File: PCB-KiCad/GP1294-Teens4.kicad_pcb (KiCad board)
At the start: 2 copper layers, 178.3 x 100.1 mm, 98 parts, among them IC1 74132D, IC3 ZXBM5210, Q1 ALS-PDIC144, SW1 SW_DPDT_x2, SW2 SW_DPDT_x2, SW3 SW_DPDT_x2, SW4 SW_DPDT_x2, SW5 SW_DPDT_x2, U10 TSOP34S40F, U3 R-78B5.0-2.0, U5 ATtiny84A-P, U6 74HC165, U7 74HC165, U8 CS8421

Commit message: Fixed merge fail.
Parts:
- removed the R2 at (104.5, 61.5)
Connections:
- U1 pad 2: F1 -> unconnected-(U1-F+-Pad2)
- U1 pad 29: F2 -> unconnected-(U1-F--Pad29)
- U1 pad 3: F1 -> unconnected-(U1-F+-Pad3)
- U1 pad 30: F2 -> unconnected-(U1-F--Pad30)
- U1 pad 31: F2 -> unconnected-(U1-F--Pad31)
- U1 pad 4: F1 -> unconnected-(U1-F+-Pad4)
- U1 pad 9: Net-(U1-TEST) -> +3.3V

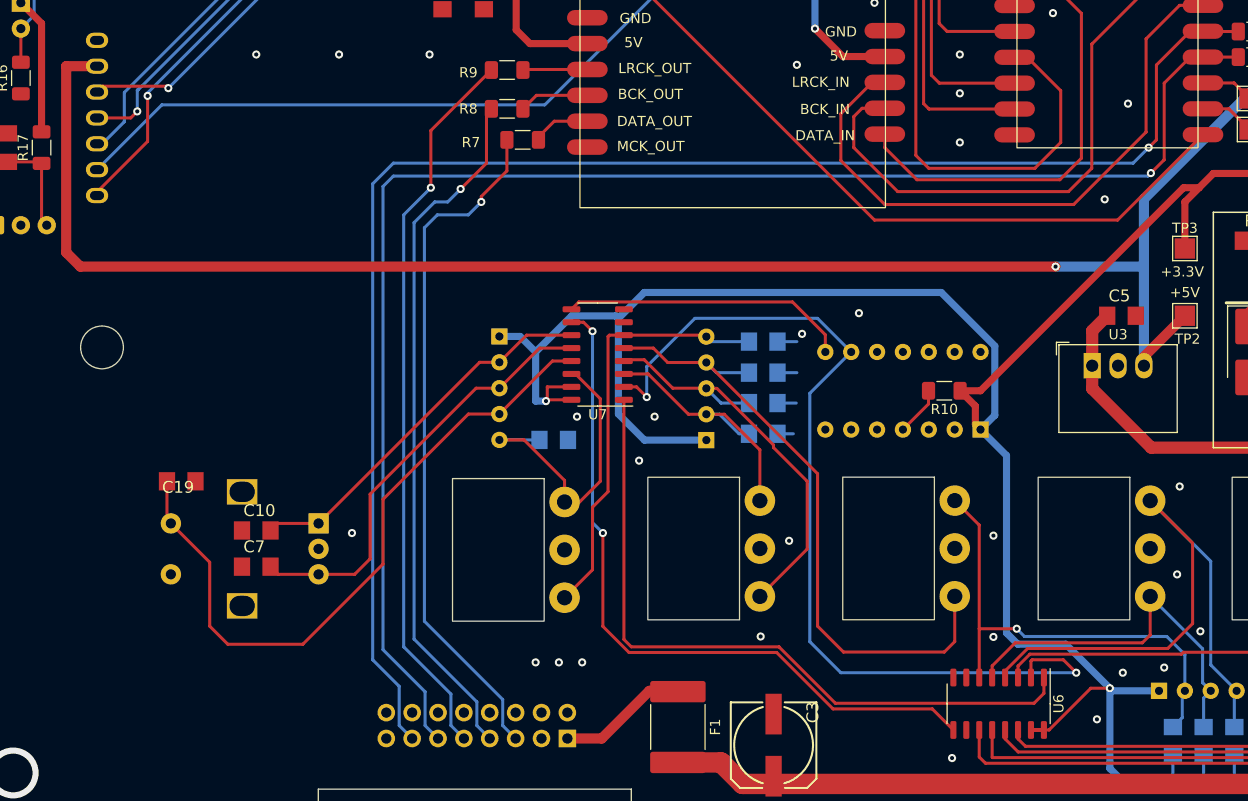
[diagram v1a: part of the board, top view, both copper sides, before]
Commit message: Fixed i2c..
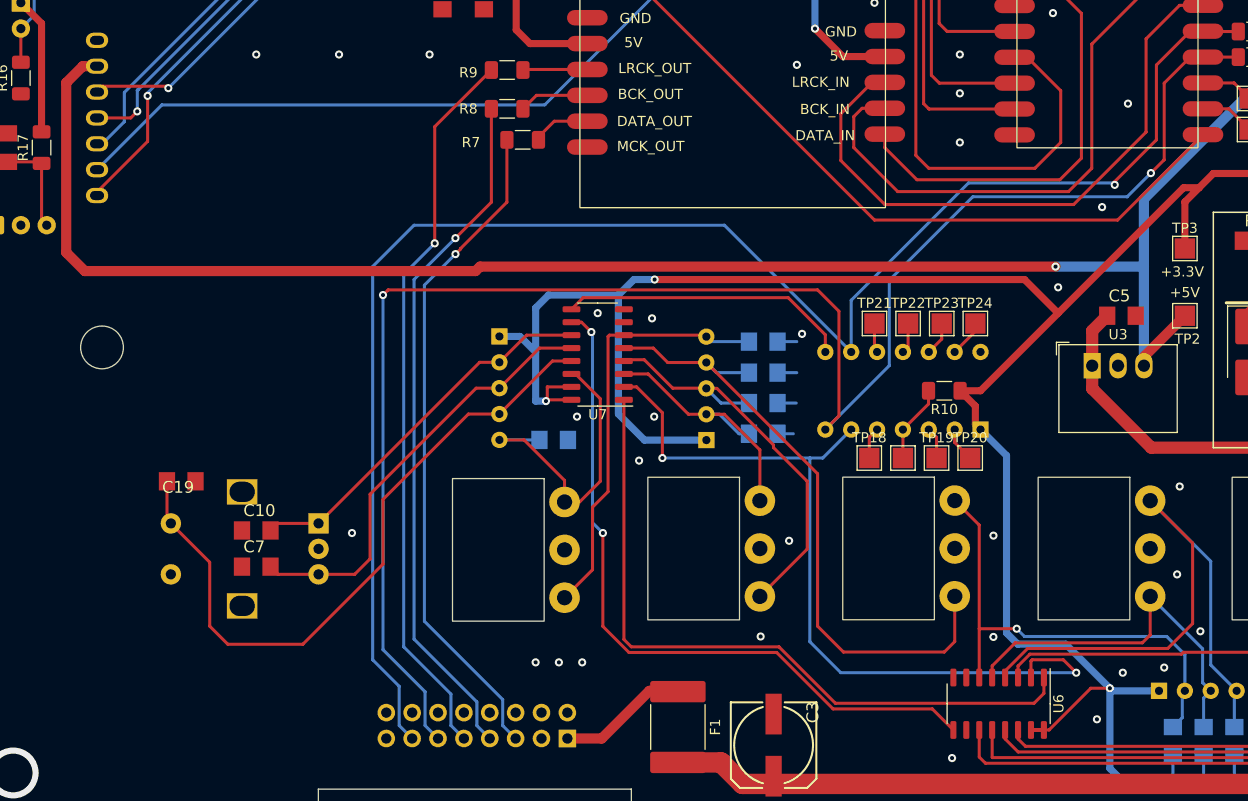
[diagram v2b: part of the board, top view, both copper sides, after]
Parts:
- added TP17: PB3, TestPoint:TestPoint_Pad_2.0x2.0mm, F.Cu at (151.4, 116.1)
- added TP18: PB2, TestPoint:TestPoint_Pad_2.0x2.0mm, F.Cu at (148.1, 116.1)
- added TP19: PB1, TestPoint:TestPoint_Pad_2.0x2.0mm, F.Cu at (154.7, 116.1)
- added TP20: PB0, TestPoint:TestPoint_Pad_2.0x2.0mm, F.Cu at (158.0, 116.1)
- added TP21: PA3, TestPoint:TestPoint_Pad_2.0x2.0mm, F.Cu at (148.6, 102.9)
- added TP22: PA2, TestPoint:TestPoint_Pad_2.0x2.0mm, F.Cu at (151.9, 102.9)
- added TP23: PA1, TestPoint:TestPoint_Pad_2.0x2.0mm, F.Cu at (155.2, 102.9)
- added TP24: PA0, TestPoint:TestPoint_Pad_2.0x2.0mm, F.Cu at (158.5, 102.9)
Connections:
- net Net-(U5-PA5) renamed /inputs/SIN
- R11 pad 2: /SCL -> SCL
- R12 pad 2: /SDA -> SDA
- U2 pad 18: /SDA -> SDA
- U2 pad 19: /SCL -> SCL
- U4 pad 11: /SDA -> SDA
- U4 pad 13: /SCL -> SCL
- U5 pad 10: unconnected-(U5-PA3-Pad10) -> Net-(U5-PA3)
- U5 pad 11: unconnected-(U5-PA2-Pad11) -> Net-(U5-PA2)
- U5 pad 12: /inputs/SCL -> Net-(U5-PA1)
- U5 pad 13: /inputs/SDA -> Net-(U5-AREF/PA0)
- U5 pad 2: unconnected-(U5-XTAL1/PB0-Pad2) -> Net-(U5-XTAL1/PB0)
- U5 pad 3: unconnected-(U5-XTAL2/PB1-Pad3) -> Net-(U5-XTAL2/PB1)
- U5 pad 5: unconnected-(U5-PB2-Pad5) -> Net-(U5-PB2)
- U5 pad 6: unconnected-(U5-PA7-Pad6) -> /inputs/SCLK
- U5 pad 7: unconnected-(U5-PA6-Pad7) -> SDA
- U5 pad 9: Net-(U5-PA4) -> SCL
- U6 pad 2: Net-(U5-PA4) -> /inputs/SCLK
- U7 pad 2: Net-(U5-PA4) -> /inputs/SCLK
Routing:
- net SDA: track 0.00 -> 168.8 mm, vias 0 -> 2
- net SCL: track 0.00 -> 160.5 mm, vias 0 -> 1
- net /SCL: track 151.6 -> 0.00 mm, vias 1 -> 0
- net /SDA: track 150.1 -> 0.00 mm, vias 1 -> 0
- net Net-(U5-PA4): track 93.3 -> 0.00 mm, vias 2 -> 0
- net /inputs/SCLK: track 0.00 -> 81.1 mm, vias 0 -> 2
- net Net-(U5-AREF/PA0): track 0.00 -> 3.64 mm
- net Net-(U5-XTAL1/PB0): track 0.00 -> 3.43 mm
- net Net-(U5-PA1): track 0.00 -> 3.32 mm
- net Net-(U5-XTAL2/PB1): track 0.00 -> 3.11 mm
- net Net-(U5-PB2): track 0.00 -> 3.11 mm
- net Net-(U5-PA2): track 0.00 -> 3.00 mm
- net Net-(U5-PA3): track 0.00 -> 2.90 mm
- net Net-(U5-~{RESET}/PB3): track 4.85 -> 7.65 mm
- net Net-(U4-MP8/MDO): track 67.6 -> 65.8 mm
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
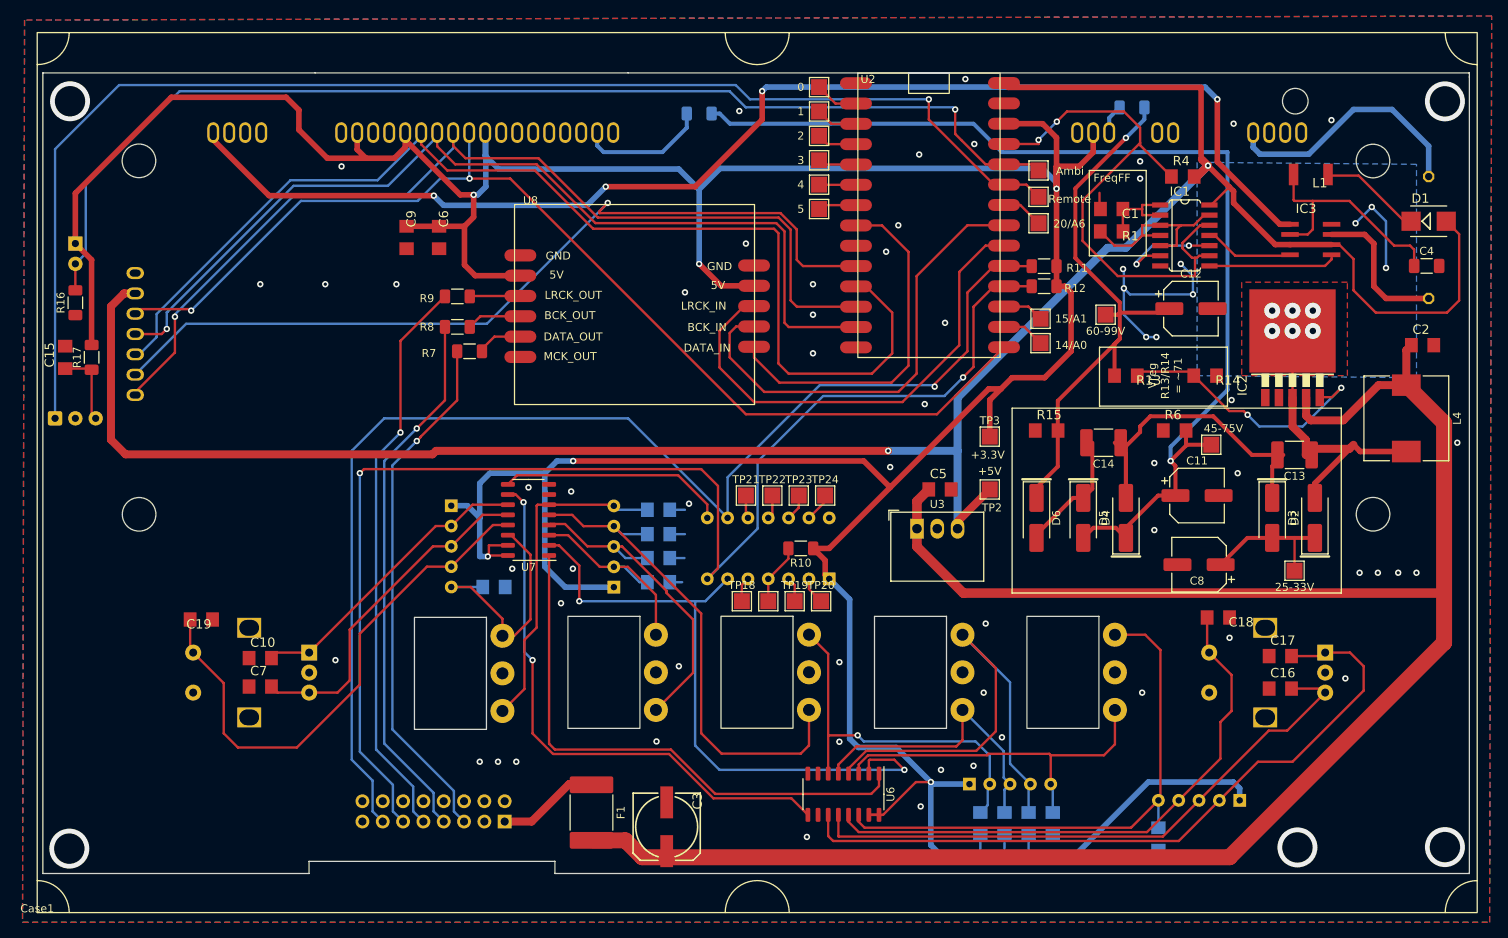
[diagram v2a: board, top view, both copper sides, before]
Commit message: Some silkscreen fixes.
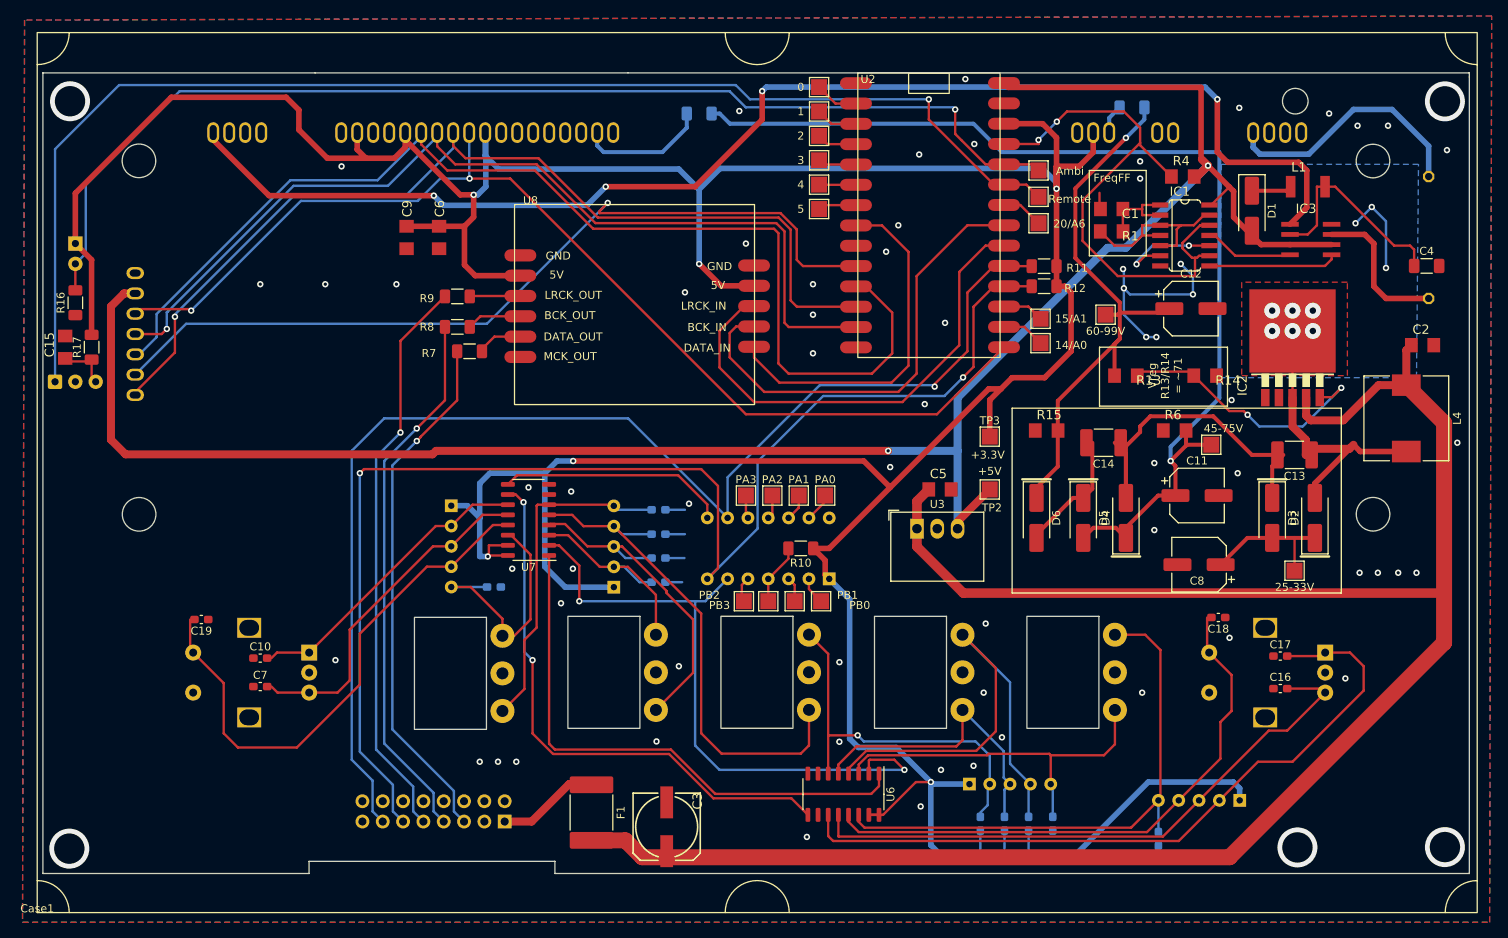
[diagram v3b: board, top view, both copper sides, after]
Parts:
- removed TP17: PB3, TestPoint:TestPoint_Pad_2.0x2.0mm
- removed TP18: PB2, TestPoint:TestPoint_Pad_2.0x2.0mm
- removed TP19: PB1, TestPoint:TestPoint_Pad_2.0x2.0mm
- removed TP20: PB0, TestPoint:TestPoint_Pad_2.0x2.0mm
- removed TP21: PA3, TestPoint:TestPoint_Pad_2.0x2.0mm
- removed TP22: PA2, TestPoint:TestPoint_Pad_2.0x2.0mm
- removed TP23: PA1, TestPoint:TestPoint_Pad_2.0x2.0mm
- removed TP24: PA0, TestPoint:TestPoint_Pad_2.0x2.0mm
- added PA0: PA0, TestPoint:TestPoint_Pad_2.0x2.0mm, F.Cu at (158.5, 102.9)
- added PA1: PA1, TestPoint:TestPoint_Pad_2.0x2.0mm, F.Cu at (155.2, 102.9)
- added PA2: PA2, TestPoint:TestPoint_Pad_2.0x2.0mm, F.Cu at (151.9, 102.9)
- added PA3: PA3, TestPoint:TestPoint_Pad_2.0x2.0mm, F.Cu at (148.6, 102.9)
- added PB0: PB0, TestPoint:TestPoint_Pad_2.0x2.0mm, F.Cu at (158.0, 116.1)
- added PB1: PB1, TestPoint:TestPoint_Pad_2.0x2.0mm, F.Cu at (154.7, 116.1)
- added PB2: PB2, TestPoint:TestPoint_Pad_2.0x2.0mm, F.Cu at (148.3, 116.1)
- added PB3: PB3, TestPoint:TestPoint_Pad_2.0x2.0mm, F.Cu at (151.4, 116.1)
- C10, C16, C17, C18, C19, C20, C21, C22, C23, C24, C25, C26, C27, C28, C29, C7: footprint VFD-Power:C1206 -> Capacitor_SMD:C_0603_1608Metric_Pad1.08x0.95mm_HandSolder
- D1: value DIODE-SMB -> 1N5818; footprint VFD-Power:SMB -> Diode_SMD:D_SMA_Handsoldering
- moved D1 22.1 mm to (211.8, 67.3), turned to -90 degrees
- moved U10 4.57 mm to (62.2, 88.6)
- moved L1 1.57 mm to (218.8, 64.3), turned to 0 degrees
- moved C15 1.27 mm to (63.5, 84.3)
- moved R17 1.27 mm to (66.8, 84.3)
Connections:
- L1 pad 1: Net-(D1-PadC) -> Net-(D1-K)
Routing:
- net +5V: track 288.5 -> 256.6 mm
- net Net-(D1-PadC): track 12.8 -> 0.00 mm
- net F1: track 159.3 -> 165.5 mm
- net Net-(D1-K): track 0.00 -> 5.05 mm
- net Net-(U10-OUT): track 167.2 -> 162.6 mm
- net Net-(IC3-VM): track 29.5 -> 26.1 mm
- net Net-(U10-Vs): track 9.64 -> 6.53 mm
- net VHG: track 135.9 -> 134.5 mm
- net +3.3V: track 518.0 -> 516.7 mm
- net GND: vias 69 -> 72

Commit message: Beauty fixes
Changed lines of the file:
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@@
     (property "Sheetname" "Power")
     (attr smd)
-    (fp_text reference "R1" (at -1.27 -1.27 180) (layer "F.SilkS")
+    (fp_text reference "R1" (at 2.794 -3.048 180) (layer "F.SilkS")
         (effects (font (size 1.1684 1.1684) (thickness 0.1016)) (justify left bottom))
     )
-    (fp_text value "2.7k" (at -1.27 2.54 180) (layer "F.Fab")
+    (fp_text value "2.7k" (at -0.44 -2.9 180) (layer "F.Fab")
         (effects (font (size 1.1684 1.1684) (thickness 0.1016)) (justify left bottom))
     )
@@
     (property "Sheetname" "Power")
     (attr smd)
-    (fp_text reference "R4" (at -1.27 -1.27) (layer "F.SilkS")
+    (fp_text reference "R4" (at -2.95 -1.492) (layer "F.SilkS")
         (effects (font (size 1.1684 1.1684) (thickness 0.1016)) (justify left bottom))
     )
-    (fp_text value "2.7k" (at -1.27 2.54) (layer "F.Fab")
+    (fp_text value "2.7k" (at -0.2 -1.492) (layer "F.Fab")
         (effects (font (size 1.1684 1.1684) (thickness 0.1016)) (justify left bottom))
     )
@@
         (effects (font (size 1.143 1.143) (thickness 0.127)) (justify left bottom))
     )
-    (fp_text value "74132D" (at -3.175 0.762 90) (layer "F.Fab")
+    (fp_text value "74132D" (at -3.175 0.204 90) (layer "F.Fab")
         (effects (font (size 1.143 1.143) (thickness 0.127)) (justify right bottom))
     )
@@
         (effects (font (size 1.1684 1.1684) (thickness 0.1016)) (justify left bottom))
     )
-    (fp_text value "ZXBM5210" (at 4.445 1.905) (layer "F.Fab")
+    (fp_text value "ZXBM5210" (at 4.445 4.452) (layer "F.Fab")
         (effects (font (size 1.1684 1.1684) (thickness 0.1016)) (justify left bottom))
     )
@@
     (property "Sheetname" "Power")
     (attr smd)
-    (fp_text reference "C1" (at -1.27 -1.27 180) (layer "F.SilkS")
+    (fp_text reference "C1" (at 2.56 1.556 180) (layer "F.SilkS")
         (effects (font (size 1.1684 1.1684) (thickness 0.1016)) (justify left bottom))
     )
-    (fp_text value "4.7n" (at -1.27 2.54 180) (layer "F.Fab")
+    (fp_text value "4.7n" (at -0.44 1.556 180) (layer "F.Fab")
         (effects (font (size 1.1684 1.1684) (thickness 0.1016)) (justify left bottom))
     )
@@
   (segment (start 113.408 74.038) (end 113.408 69.212) (width 0.7) (layer "F.Cu") (net 17))
   (segment (start 185.674 56.388) (end 187.415 58.129) (width 0.7) (layer "F.Cu") (net 17))
-  (segment (start 101.092 60.706) (end 104.648 60.706) (width 0.7) (layer "F.Cu") (net 17))
+  (segment (start 110.581238 65.278) (end 110.581238 63.331238) (width 0.7) (layer "F.Cu") (net 17))
+  (segment (start 114.554 65.278) (end 110.581238 65.278) (width 0.7) (layer "F.Cu") (net 17))
   (segment (start 192 59.968) (end 192 57.5) (width 0.7) (layer "F.Cu") (net 17))
   (segment (start 106.3348 69.212) (end 110.236 69.212) (width 0.7) (layer "F.Cu") (net 17))
@@
   (segment (start 118.837 109.093) (end 116.459 109.093) (width 0.3) (layer "F.Cu") (net 17))
   (segment (start 179.07 95.504) (end 179.07 90.932) (width 0.7) (layer "F.Cu") (net 17))
-  (segment (start 104.648 60.706) (end 106 59.354) (width 0.7) (layer "F.Cu") (net 17))
   (segment (start 92.71 54.674845) (end 92.71 57.15) (width 0.7) (layer "F.Cu") (net 17))
-  (segment (start 112.878 65.278) (end 106 58.4) (width 0.7) (layer "F.Cu") (net 17))
   (segment (start 113.408 69.212) (end 110.236 69.212) (width 0.7) (layer "F.Cu") (net 17))
   (segment (start 96.266 60.706) (end 101.092 60.706) (width 0.7) (layer "F.Cu") (net 17))
   (segment (start 178.943 89.535) (end 166.624 101.854) (width 0.7) (layer "F.Cu") (net 17))
   (segment (start 187.415 76.708) (end 188.468 76.708) (width 0.7) (layer "F.Cu") (net 17))
+  (segment (start 106 60.706) (end 106 57.5) (width 0.7) (layer "F.Cu") (net 17))
   (segment (start 180.467 89.535) (end 178.943 89.535) (width 0.7) (layer "F.Cu") (net 17))
   (segment (start 179.07 90.932) (end 180.467 89.535) (width 0.7) (layer "F.Cu") (net 17))
   (segment (start 190.263 61.705) (end 192 59.968) (width 0.7) (layer "F.Cu") (net 17))
+  (segment (start 101.092 60.706) (end 106 60.706) (width 0.7) (layer "F.Cu") (net 17))
   (segment (start 163.957 142.783) (end 165.735 142.783) (width 0.3) (layer "F.Cu") (net 17))
   (segment (start 100 57.5) (end 100 59.614) (width 0.7) (layer "F.Cu") (net 17))
@@
   (segment (start 114.554 65.278) (end 114.554 68.066) (width 0.7) (layer "F.Cu") (net 17))
   (segment (start 181.864 88.138) (end 180.467 89.535) (width 0.7) (layer "F.Cu") (net 17))
+  (segment (start 107.956 60.706) (end 106 60.706) (width 0.7) (layer "F.Cu") (net 17))
   (segment (start 64.77 65.081514) (end 76.765514 53.086) (width 0.7) (layer "F.Cu") (net 17))
-  (segment (start 106 58.4) (end 106 57.5) (width 0.7) (layer "F.Cu") (net 17))
-  (segment (start 114.554 65.278) (end 112.878 65.278) (width 0.7) (layer "F.Cu") (net 17))
   (segment (start 187.415 61.705) (end 187.415 64.516) (width 0.7) (layer "F.Cu") (net 17))
   (segment (start 165.227 142.783) (end 163.957 142.783) (width 0.3) (layer "F.Cu") (net 17))
@@
   (segment (start 116.459 109.093) (end 116.459 110.363) (width 0.3) (layer "F.Cu") (net 17))
   (segment (start 156.998 109.474) (end 158.496 110.972) (width 0.7) (layer "F.Cu") (net 17))
-  (segment (start 106 59.354) (end 106 57.5) (width 0.7) (layer "F.Cu") (net 17))
   (segment (start 114.754 75.384) (end 113.408 74.038) (width 0.7) (layer "F.Cu") (net 17))
   (segment (start 76.765514 53.086) (end 91.121155 53.086) (width 0.7) (layer "F.Cu") (net 17))
+  (segment (start 110.581238 63.331238) (end 107.956 60.706) (width 0.7) (layer "F.Cu") (net 17))
   (segment (start 189.23 84.836) (end 185.928 88.138) (width 0.7) (layer "F.Cu") (net 17))
   (segment (start 114.554 68.066) (end 113.408 69.212) (width 0.7) (layer "F.Cu") (net 17))
